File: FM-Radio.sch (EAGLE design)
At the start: 26 parts, among them IC1 7414N, IC2 ARDUINO-NANO, IC3 TEA5767, IC4 PT2257, IC5 PAM8403, SW1 5+2P-13.75X11.7MM

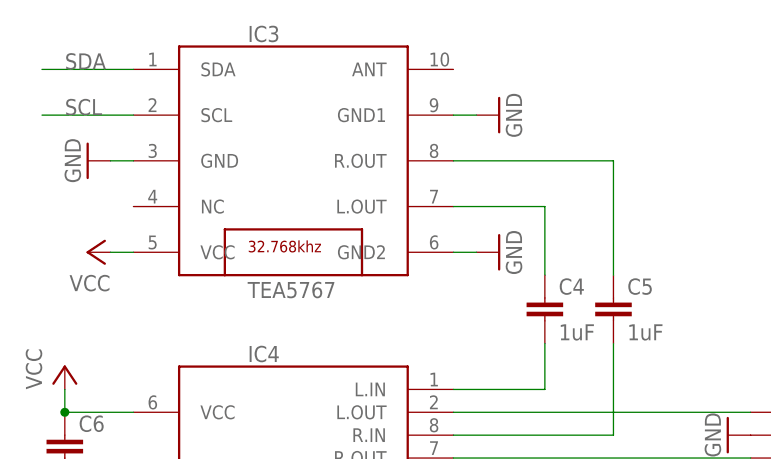
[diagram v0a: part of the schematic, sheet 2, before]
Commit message: Correct the schematic
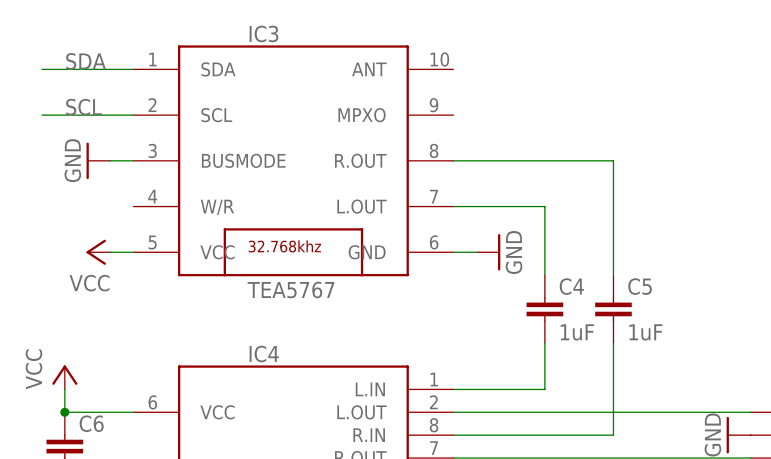
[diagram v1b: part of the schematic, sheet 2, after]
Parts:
- R7, R8: value 10K -> 4K7
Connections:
- net GND: now also IC3.BUSMODE; no longer IC3.GND1, IC3.GND2
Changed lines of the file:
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@@
 <?xml version="1.0" encoding="utf-8"?>
 <!DOCTYPE eagle SYSTEM "eagle.dtd">
-<eagle version="7.7.0">
+<eagle version="8.0.1">
 <drawing>
 <settings>
@@
 <part name="GND10" library="SaintGimp" deviceset="GND" device=""/>
 <part name="GND11" library="SaintGimp" deviceset="GND" device=""/>
-<part name="R7" library="SaintGimp" deviceset="RESISTOR-*" device="7.5MM" value="10K"/>
-<part name="R8" library="SaintGimp" deviceset="RESISTOR-*" device="7.5MM" value="10K"/>
+<part name="R7" library="SaintGimp" deviceset="RESISTOR-*" device="7.5MM" value="4K7"/>
+<part name="R8" library="SaintGimp" deviceset="RESISTOR-*" device="7.5MM" value="4K7"/>
 <part name="IC3" library="SaintGimp" deviceset="TEA5767" device=""/>
 <part name="P+6" library="SaintGimp" deviceset="VCC" device=""/>
 <part name="GND12" library="SaintGimp" deviceset="GND" device=""/>
 <part name="GND13" library="SaintGimp" deviceset="GND" device=""/>
-<part name="GND14" library="SaintGimp" deviceset="GND" device=""/>
 <part name="IC4" library="SaintGimp" deviceset="PT2257" device=""/>
 <part name="GND15" library="SaintGimp" deviceset="GND" device=""/>
@@
 <instance part="GND12" gate="1" x="-17.78" y="48.26" rot="R270"/>
 <instance part="GND13" gate="1" x="27.94" y="38.1" rot="R90"/>
-<instance part="GND14" gate="1" x="27.94" y="53.34" rot="R90"/>
 <instance part="IC4" gate="G$1" x="5.08" y="17.78"/>
 <instance part="GND15" gate="1" x="-20.32" y="10.16"/>
@@
 <net name="GND" class="0">
 <segment>
-<pinref part="IC3" gate="G$1" pin="GND"/>
+<pinref part="IC3" gate="G$1" pin="BUSMODE"/>
 <pinref part="GND12" gate="1" pin="GND"/>
 <wire x1="-12.7" y1="48.26" x2="-15.24" y2="48.26" width="0.1524" layer="91"/>
 </segment>
 <segment>
-<pinref part="IC3" gate="G$1" pin="GND2"/>
+<pinref part="IC3" gate="G$1" pin="GND"/>
 <pinref part="GND13" gate="1" pin="GND"/>
 <wire x1="22.86" y1="38.1" x2="25.4" y2="38.1" width="0.1524" layer="91"/>
 </segment>
 <segment>
-<pinref part="GND14" gate="1" pin="GND"/>
-<pinref part="IC3" gate="G$1" pin="GND1"/>
-<wire x1="25.4" y1="53.34" x2="22.86" y2="53.34" width="0.1524" layer="91"/>
-</segment>
-<segment>
